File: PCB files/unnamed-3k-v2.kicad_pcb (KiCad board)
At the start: 2 copper layers, 59.3 x 63 mm, 31 parts, among them SW1 SW_Push, U1 ATmega32U2-AU, U2 PRTR5V0U2X, Y1 Crystal_GND24_Small

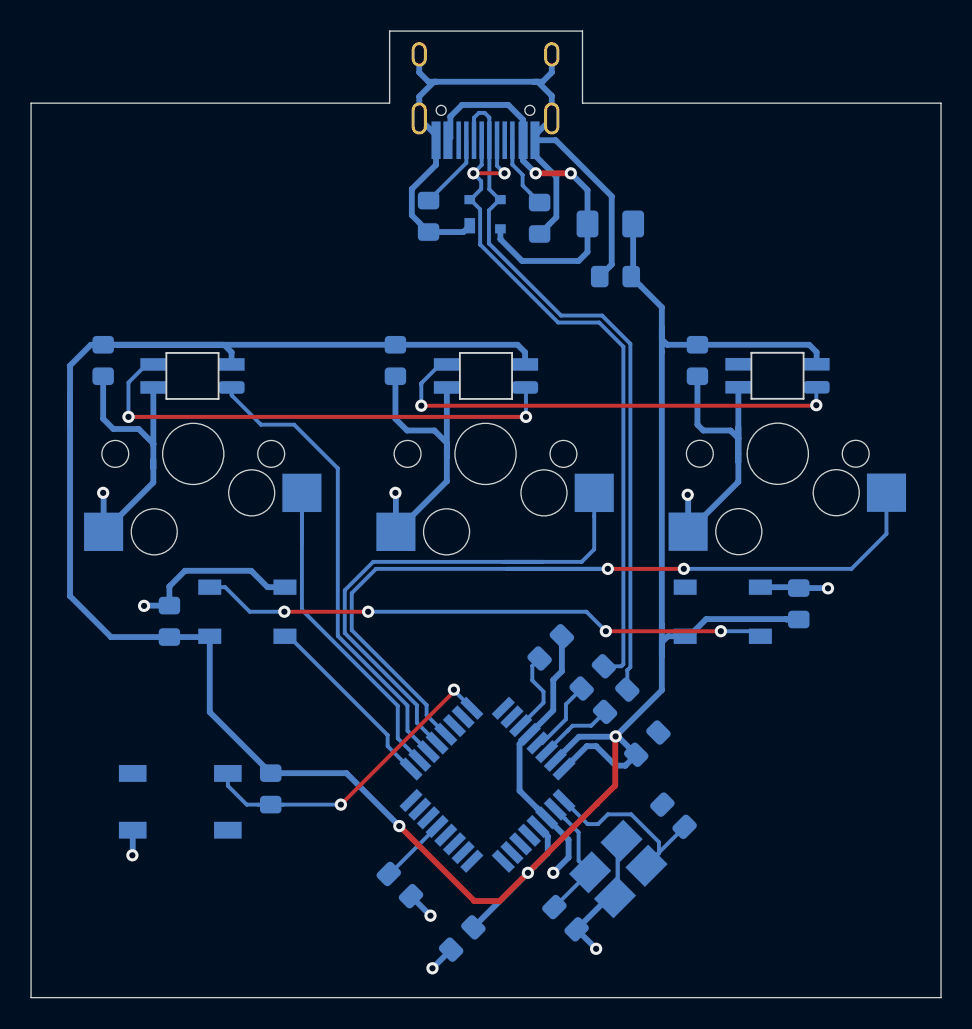
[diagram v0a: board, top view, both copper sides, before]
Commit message: Fixed PCB and firmware
Removed in-key RGB and swapped south facing hotswap sockets to north facing
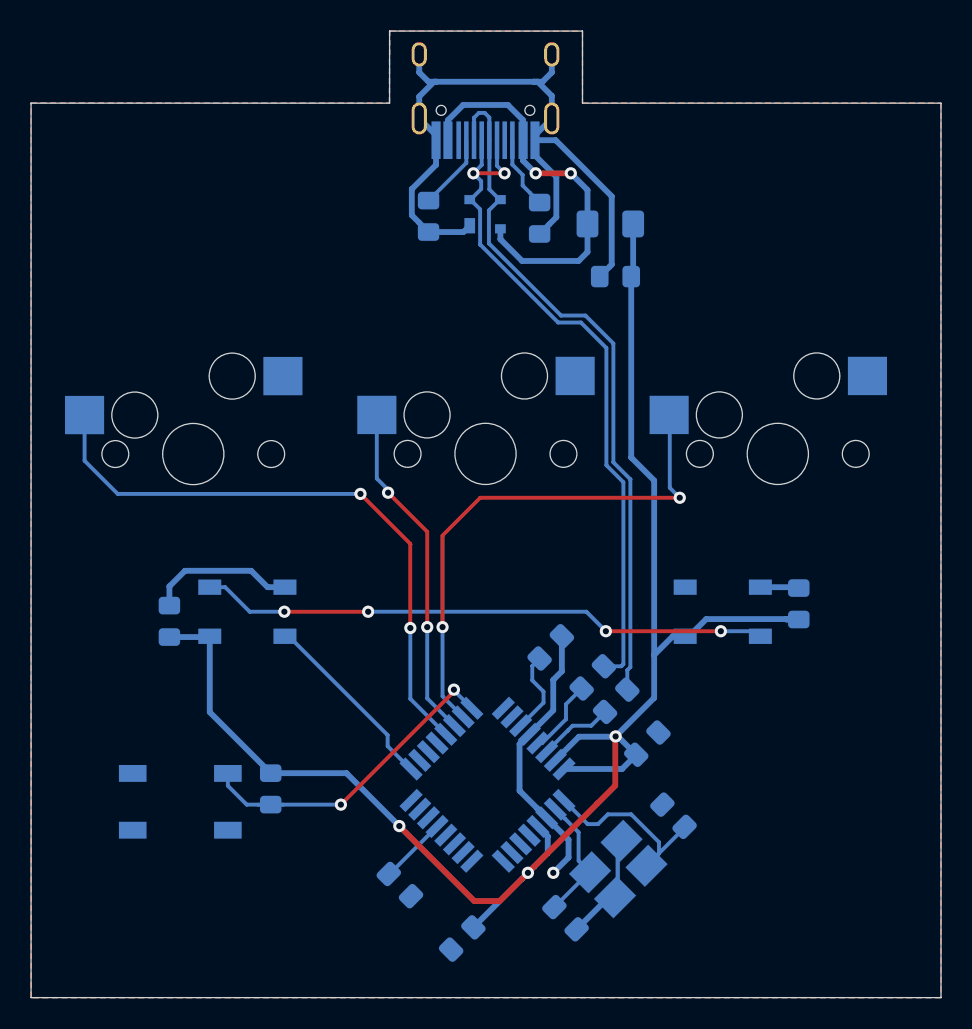
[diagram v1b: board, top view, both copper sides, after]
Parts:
- removed C7, C8, C9: 0.1uF, Capacitor_SMD:C_0805_2012Metric_Pad1.15x1.40mm_HandSolder
- removed D1, D2, D3: SK6812MINI, Keebio-Parts:SK6812-MINI-E
- R4: value R_Small -> 10k
- moved MX1 38.1 mm to (112.2, 87.6), turned to 0 degrees
- moved MX3 38.1 mm to (74.1, 87.6), turned to 0 degrees
- turned MX2 to 0 degrees
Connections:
- D5 pad 2: Net-(D5-Pad2) -> unconnected-(D5-Pad2)
- U1 pad 10: Net-(U1-Pad10) -> unconnected-(U1-Pad10)
- U1 pad 11: Net-(U1-Pad11) -> unconnected-(U1-Pad11)
- U1 pad 12: Net-(U1-Pad12) -> unconnected-(U1-Pad12)
- U1 pad 14: Net-(U1-Pad14) -> unconnected-(U1-Pad14)
- U1 pad 15: Net-(U1-Pad15) -> unconnected-(U1-Pad15)
- U1 pad 16: Net-(U1-Pad16) -> unconnected-(U1-Pad16)
- U1 pad 18: COL0 -> unconnected-(U1-Pad18)
- U1 pad 19: SWITCHLED -> unconnected-(U1-Pad19)
- U1 pad 20: COL1 -> unconnected-(U1-Pad20)
- U1 pad 22: Net-(U1-Pad22) -> COL1
- U1 pad 23: Net-(U1-Pad23) -> COL0
- U1 pad 25: Net-(U1-Pad25) -> unconnected-(U1-Pad25)
- U1 pad 26: Net-(U1-Pad26) -> unconnected-(U1-Pad26)
- U1 pad 5: Net-(U1-Pad5) -> unconnected-(U1-Pad5)
- U1 pad 6: Net-(U1-Pad6) -> unconnected-(U1-Pad6)
- U1 pad 7: Net-(U1-Pad7) -> unconnected-(U1-Pad7)
- U1 pad 8: Net-(U1-Pad8) -> unconnected-(U1-Pad8)
- U1 pad 9: Net-(U1-Pad9) -> unconnected-(U1-Pad9)
- USB1 pad 3: Net-(USB1-Pad3) -> unconnected-(USB1-Pad3)
- USB1 pad 9: Net-(USB1-Pad9) -> unconnected-(USB1-Pad9)
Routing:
- net +5V: track 190.9 -> 111.3 mm
- net GND: track 161.7 -> 88.1 mm, vias 10 -> 1
- net Net-(D1-Pad1): track 32.2 -> 0.00 mm, vias 2 -> 0
- net Net-(D2-Pad1): track 30.6 -> 0.00 mm, vias 2 -> 0
- net SWITCHLED: track 30.3 -> 0.00 mm
- net COL2: track 57.5 -> 39.8 mm
- net COL1: track 36.0 -> 22.3 mm, vias 0 -> 2
- net COL0: track 23.9 -> 34.5 mm, vias 0 -> 2
- net D+: track 46.3 -> 45.6 mm
- net D-: track 46.1 -> 45.5 mm
- added copper zone on B.Cu, net GND
- added copper zone on F.Cu, net GND
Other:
- net class Default removed
- net class Power removed
